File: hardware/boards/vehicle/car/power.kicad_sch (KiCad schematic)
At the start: 10 parts, among them U2 AMS1117CD-3.3, U3 AMS1117CD-5.0

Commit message: car schematic
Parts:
- removed C10, C11, C6, C7: 10uF, symbol Device:C
- removed C12, C5, C8, C9: 100nF, symbol Device:C
- removed U2: AMS1117CD-3.3, Package_TO_SOT_SMD:TO-252-3_TabPin2, symbol Regulator_Linear:AMS1117CD-3.3
- removed U3: AMS1117CD-5.0, Package_TO_SOT_SMD:TO-252-3_TabPin2, symbol Regulator_Linear:AMS1117CD-5.0
- added C19, C43: 10uF, symbol common:Capacitor
- added C20, C21, C42: 100nF, symbol common:Capacitor
- added C22, C23, C41: 22uF, symbol common:Capacitor
- added C24: 75pF, symbol common:Capacitor
- added D12: 1N400x, symbol common:Diode
- added L1: 10uH, symbol common:Inductor
- added R23: 511K, symbol common:Resistor
- added R25: 105K, symbol common:Resistor
- added R29: 43.2K, symbol common:Resistor
- added R30: 5.76K, symbol common:Resistor
- added R31: 1R, symbol common:Resistor
- added U4: TPS54302, symbol air_sens_lib:TPS54302
- added U5: AMS1117-3.3, Package_TO_SOT_SMD:SOT-223-3_TabPin2, symbol Regulator_Linear:AMS1117-3.3
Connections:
- net 12V: now also C19.2, C20.2, R23.2, U4.3 (VIN)
- net 3V3: now also C43.2, D12., U5.2 (VO)
- net 5V: now also C22.1, C23.2, C24.2, C41.2, C42.2, D12., L1.2, R29.2, U5.3 (VI)
- net GND: now also C19.1, C20.1, C22.2, C23.1, C41.1, C42.1, R25.1, R30.1, R31.1, U4.1 (GND), U5.1 (GND)
- new net: C24.1, R29.1, R30.2, U4.4 (FB)
- new net: R23.1, R25.2, U4.5 (EN)
- new net: C21.2, L1.1, U4.2 (SW)
- new net: C21.1, U4.6 (BOOT)
- new net: C43.1, R31.2
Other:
- note added: "3V3 @ 1A"
- note added: "5V @ 3A"
- note added: "L1 needs a saturation current of at least 4A"
- note added: "This will get hot. We'll have to add a heatsink"
- note added: "We'll need a large copper pour (Power Ground) on both the top and bottom layers of the pcb for heat dissipation"

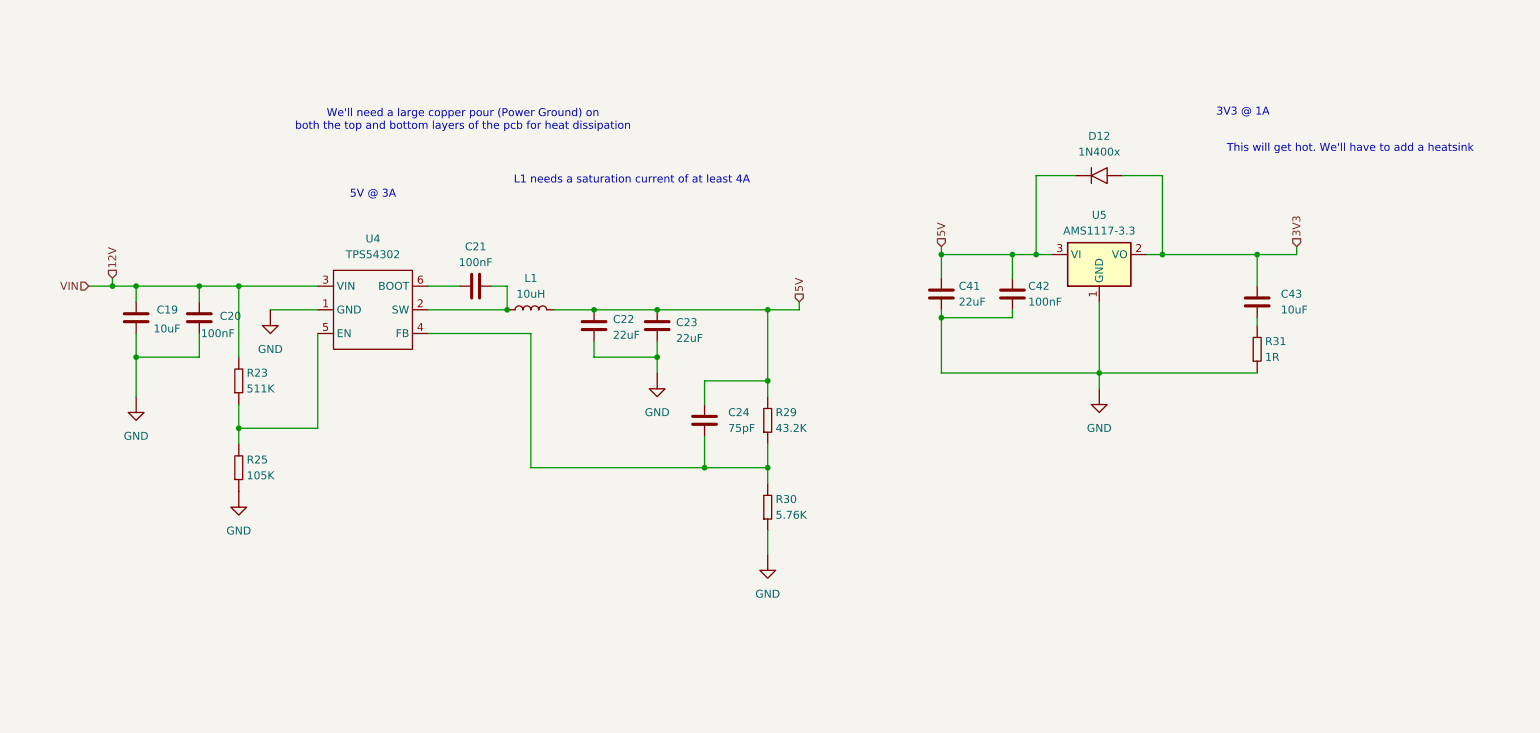
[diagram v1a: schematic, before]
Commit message: added all footprints for lidar and car
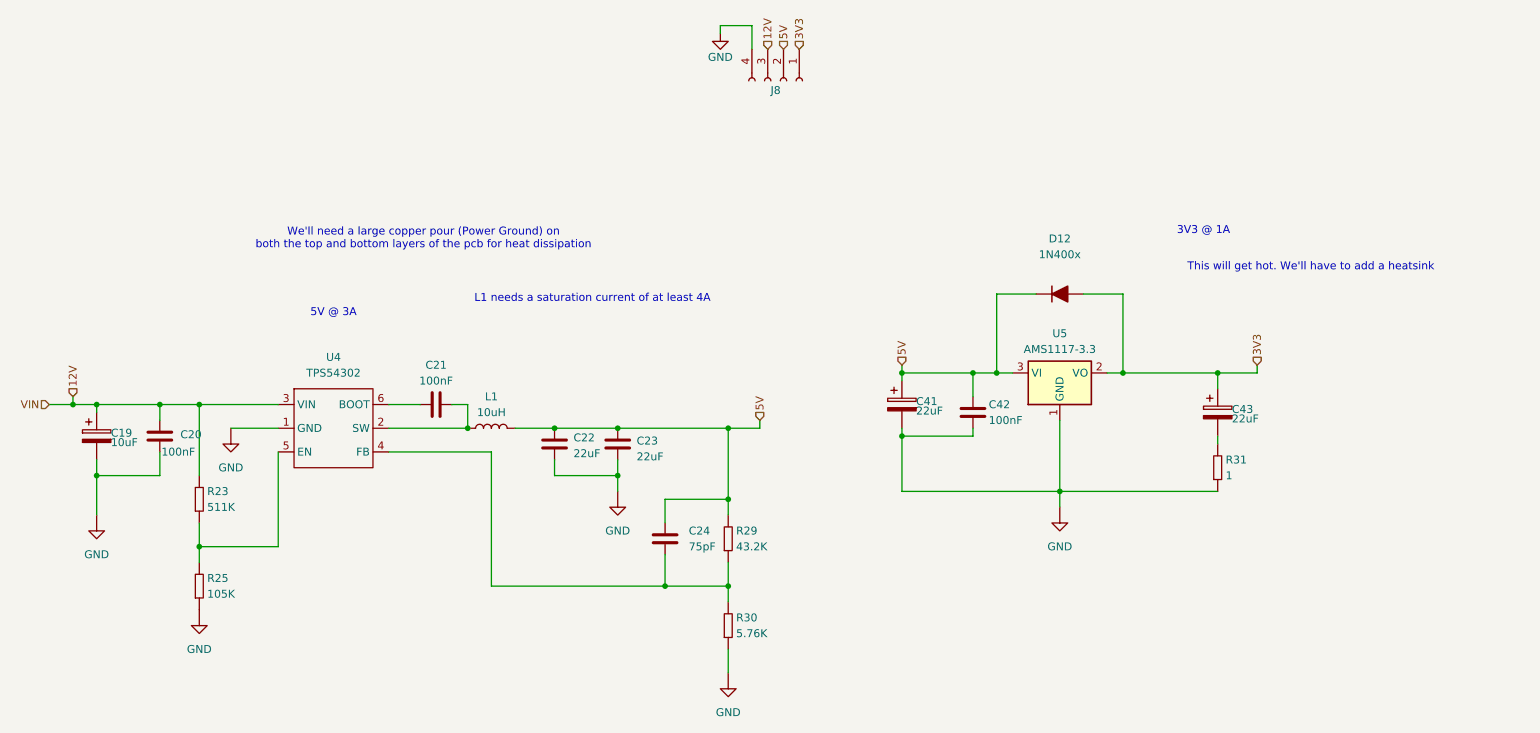
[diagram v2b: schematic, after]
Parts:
- removed C19, C43: 10uF, symbol common:Capacitor
- removed C41: 22uF, symbol common:Capacitor
- added C19: 10uF, Capacitor_THT:CP_Radial_D5.0mm_P2.00mm, symbol Device:C_Polarized
- added C41, C43: 22uF, Capacitor_THT:CP_Radial_D5.0mm_P2.00mm, symbol Device:C_Polarized
- added J8: Conn_01x04_Socket, Connector_PinHeader_2.54mm:PinHeader_1x04_P2.54mm_Vertical, symbol Connector:Conn_01x04_Socket
- C20, C21, C22, C23, C24, C42: footprint (none) -> Capacitor_SMD:C_0603_1608Metric_Pad1.08x0.95mm_HandSolder
- D12: footprint (none) -> Diode_THT:D_DO-41_SOD81_P2.54mm_Vertical_AnodeUp
- L1: footprint (none) -> Inductor_SMD:L_0603_1608Metric_Pad1.05x0.95mm_HandSolder
- R23, R25, R29, R30: footprint (none) -> Resistor_SMD:R_0603_1608Metric_Pad0.98x0.95mm_HandSolder
- R31: value 1R -> 1; footprint (none) -> Resistor_SMD:R_0603_1608Metric_Pad0.98x0.95mm_HandSolder
- U4: footprint (none) -> Package_TO_SOT_SMD:TSOT-23-6_HandSoldering
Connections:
- net 12V: now also C19.1, J8.3 (Pin_3)
- net 3V3: now also D12.2 (A), C43.1, J8.1 (Pin_1); no longer D12.
- net 5V: now also D12.1 (K), C41.1, J8.2 (Pin_2); no longer D12.
- net GND: now also C19.2, C41.2, J8.4 (Pin_4)
- net at R31.2: now also C43.2
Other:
- moved on the sheet: C20, C21, C22, C23, C24, C42, L1, R23, R25, R29, R30, R31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

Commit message: edited inductor footprint for car and export gerber for lidar
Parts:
- L1: footprint Inductor_SMD:L_0603_1608Metric_Pad1.05x0.95mm_HandSolder -> Connector_PinHeader_2.54mm:PinHeader_1x02_P2.54mm_Vertical
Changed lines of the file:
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@@
 			)
 		)
-		(property "Footprint" "Inductor_SMD:L_0603_1608Metric_Pad1.05x0.95mm_HandSolder"
+		(property "Footprint" "Connector_PinHeader_2.54mm:PinHeader_1x02_P2.54mm_Vertical"
 			(at 110.49 109.22 0)
 			(effects
